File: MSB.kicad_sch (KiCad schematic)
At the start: 25 parts, among them J1 22-05-3021, J2 22-05-3021, J3 90120-0763, J4 90120-0763, J5 22-05-3021, P1 22-27-2041, P2 22-27-2041, P3 61300811121, Q1 FDN5632N-F085, Q2 FDN5632N-F085, U1 MSP430FR2355TPTR, U2 LD1117S33TR

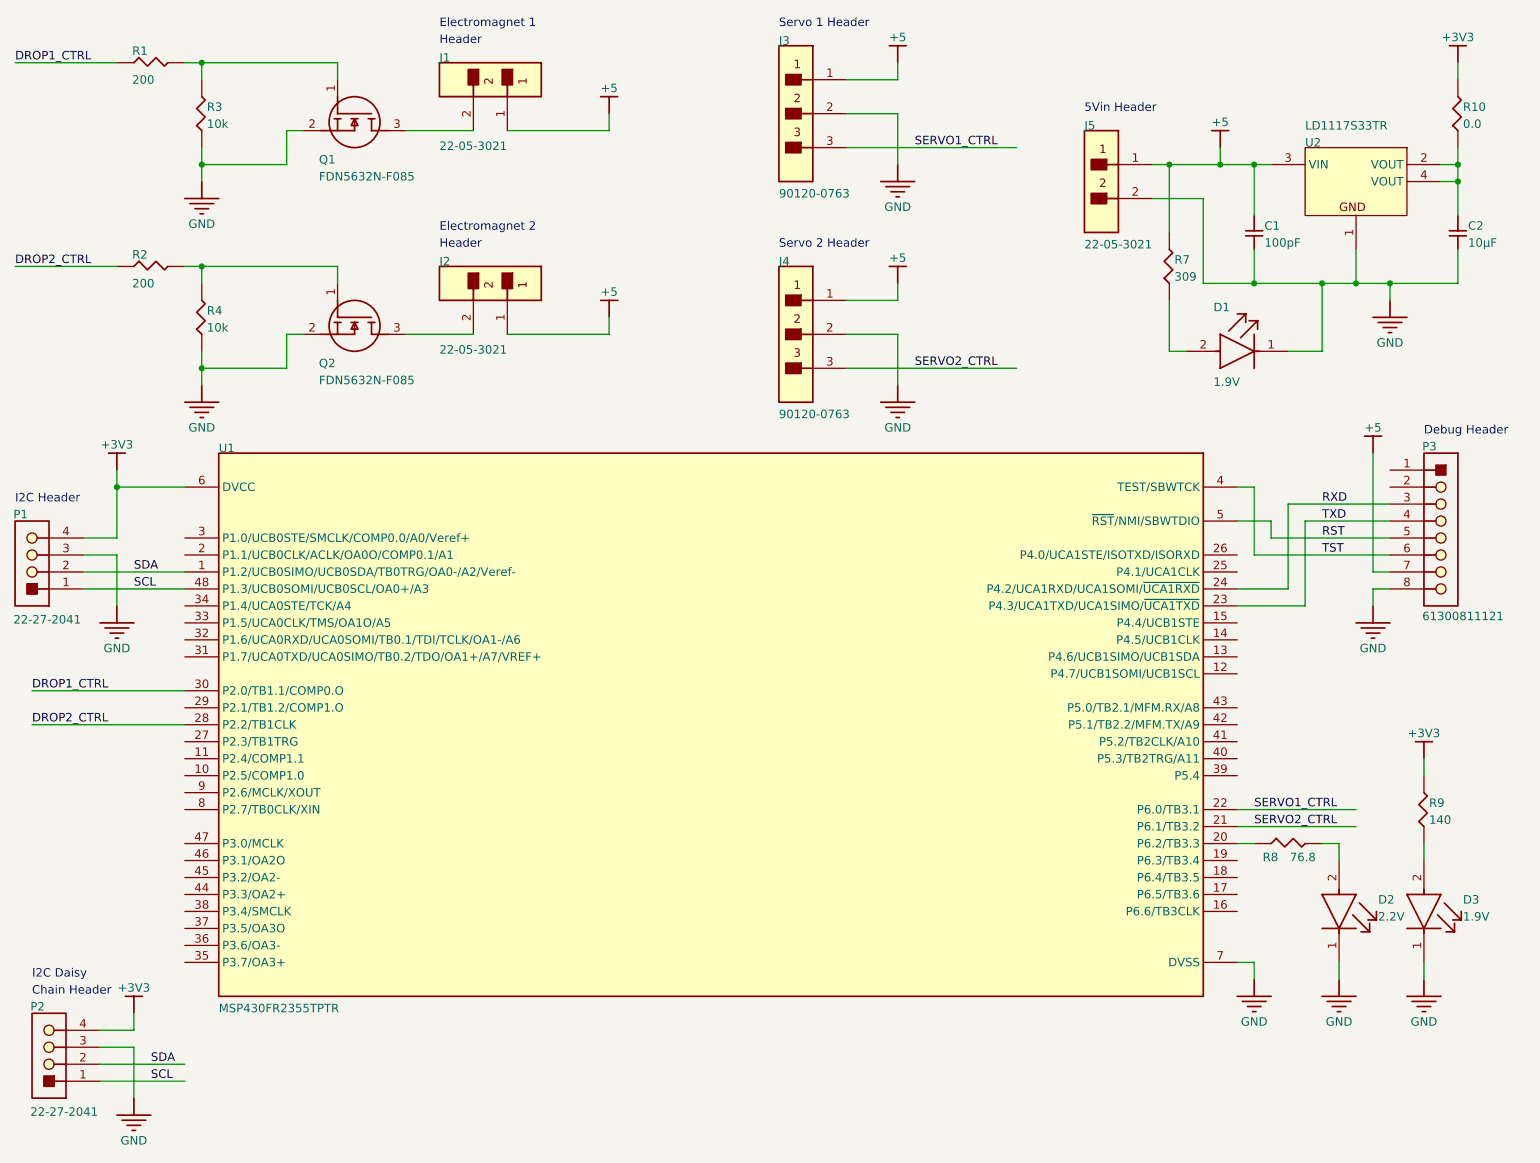
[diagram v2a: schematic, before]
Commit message: Changed MSP430 to STM32
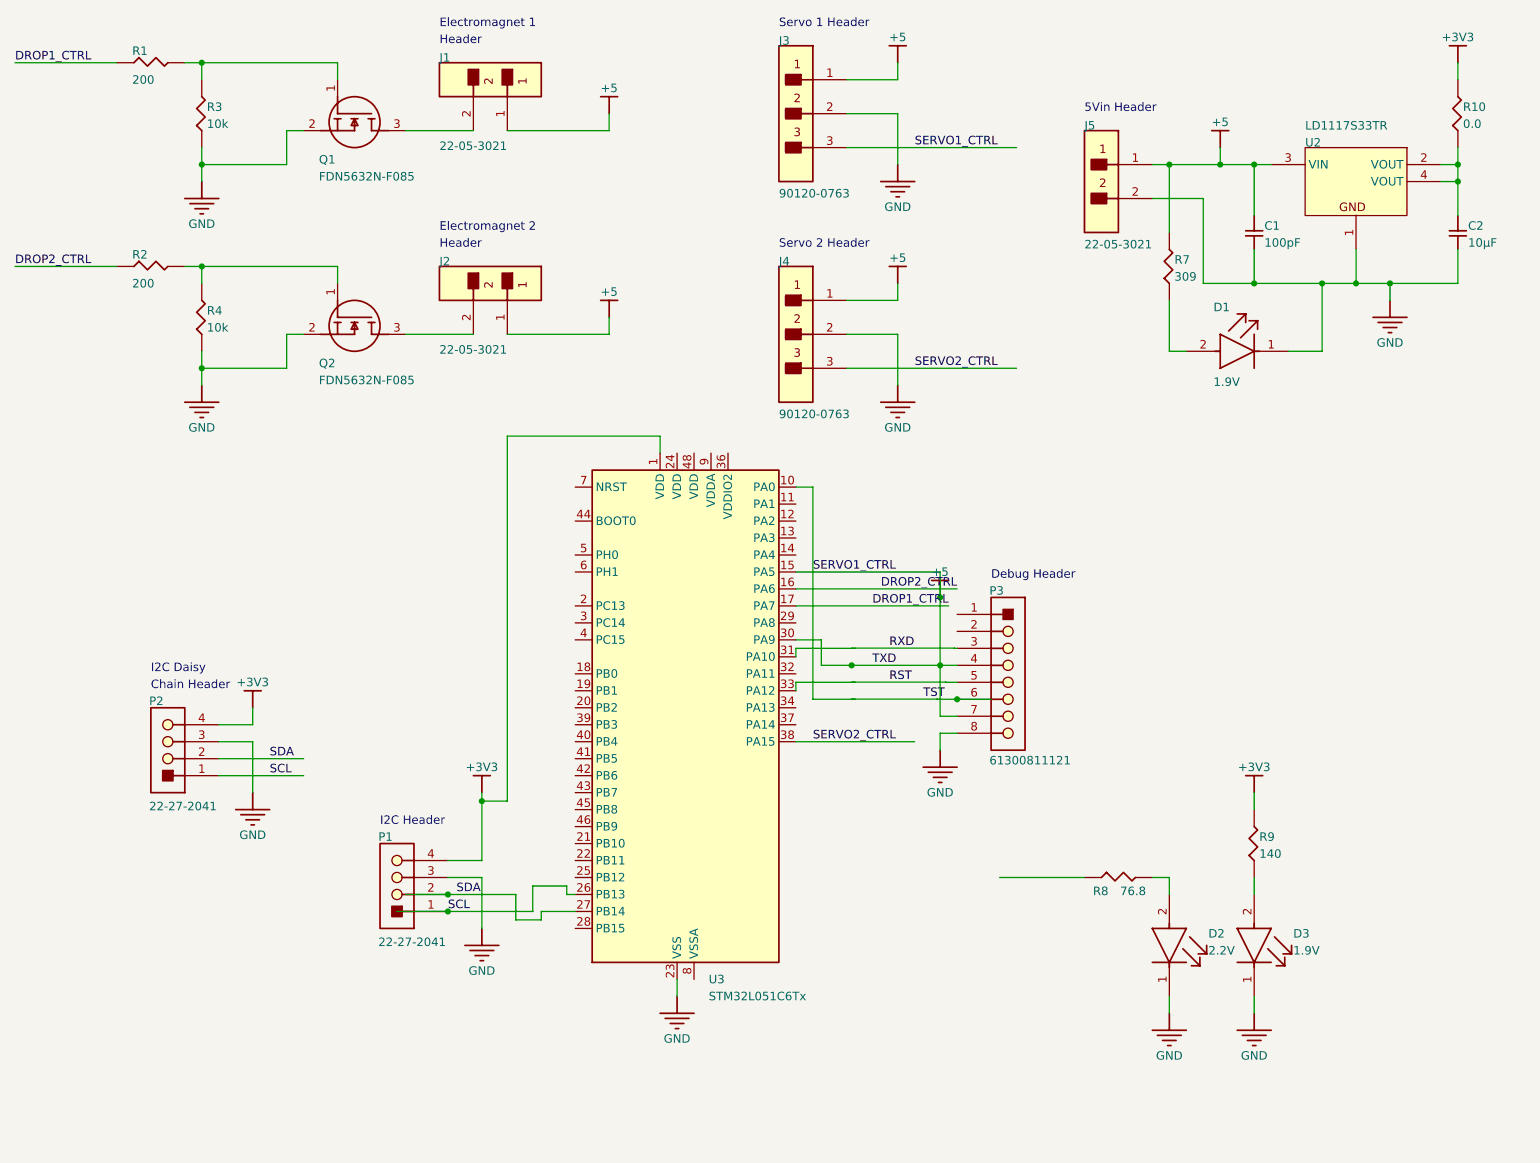
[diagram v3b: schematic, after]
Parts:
- removed U1: MSP430FR2355TPTR, AltiumImport:FP-PT0048A-MFG, symbol MSB-altium-import:root_0_bd983ca6877cdd146f198514b3acb3b
- added U3: STM32L051C6Tx, Package_QFP:LQFP-48_7x7mm_P0.5mm, symbol MCU_ST_STM32L0:STM32L051C6Tx
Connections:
- net SERVO1_CTRL is gone; now on net +5: J3.3
- net TXD is gone; now on net +5: P3.4
- net +3V3: now also U3.1 (VDD)
- net +5: now also U3.10 (PA0), U3.15 (PA5), U3.30 (PA9)
- net DROP1_CTRL: now also U3.17 (PA7)
- net DROP2_CTRL: now also U3.16 (PA6)
- net GND: now also U3.23 (VSS), U3.35 (VSS), U3.47 (VSS)
- net RST: no longer P3.5
- net RXD: no longer P3.3
- net SCL: now also U3.26 (PB13)
- net SDA: now also U3.27 (PB14)
- net SERVO2_CTRL: now also U3.38 (PA15)
- net TST: no longer P3.6
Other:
- moved on the sheet: D2, D3, P1, P2, P3, R8, R9

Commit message: Update STM32
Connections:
- net +3V3: no longer U3.1 (VDD)
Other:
- moved on the sheet: P2
